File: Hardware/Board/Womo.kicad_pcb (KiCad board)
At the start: 4 copper layers, 255 x 150 mm, 465 parts, among them IC1 SPSGRFC-868, IC200 BTS6143D, IC201 BTS6143D, IC203 BTS6143D, IC204 BTS6143D, J1 USB_B_Micro, J2 Conn_ARM_JTAG_SWD_20, J3 SD_Card, J300 734-264, J301 733-368, J302 733-368, J303 733-368, J304 Truma, J305 Dormetic, J306 733-366, J307 733-366, J308 733-366, J309 733-366, J310 733-370, J311 734-163, J312 734-163, J313 734-163, J314 734-163, J315 734-168, J316 733-363, J317 RJ45_Shielded, J318 Spare, J319 SENSOR, J320 Raspberry_Pi_2_3, J321 Wasser, J322 Abwasser, J323 733-370, J324 Waveshare IoT Hat, J325 734-168, J326 733-366, J400 USB_B_Micro, J401 RJ45_Shielded, J500 SENSOR, K300 5-1393243-2, K301 5-1393243-2, K302 5-1393243-2, K303 5-1393243-2, Q100 2N7002, Q102 2N7002, Q103 2N7002, Q104 2N7002, Q200 2N7002, Q201 2N7002, Q202 2N7002, Q203 2N7002, SW1 Boot, SW3 Reset, U1 STM32L476ZGTx, U100 MAX17572, U101 MAX17572, U102 MAX17572, U104 MAX17574, U105 MAX17574, U2 M25Q128A, U200 SN74LV4052A, U201 TJA1029T, U202 TJA1029T, U203 TJA1029T, U204 TJA1029T, U205 SN74LV4052A, U206 SN74LV4052A, U207 MAX3072E, U208 MAX3072E, U209 MAX3072E, U210 MAX3072E, U211 MAX11615, U212 PCF8574A, U213 TJA1049T-3, U214 DS2482S-800+, U215 SN74LV4052A, U216 Si8642BB-B-IS1, U217 Si8642BB-B-IS1, U3 24AA02UID, U300 max4896atp+, U301 max4896atp+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

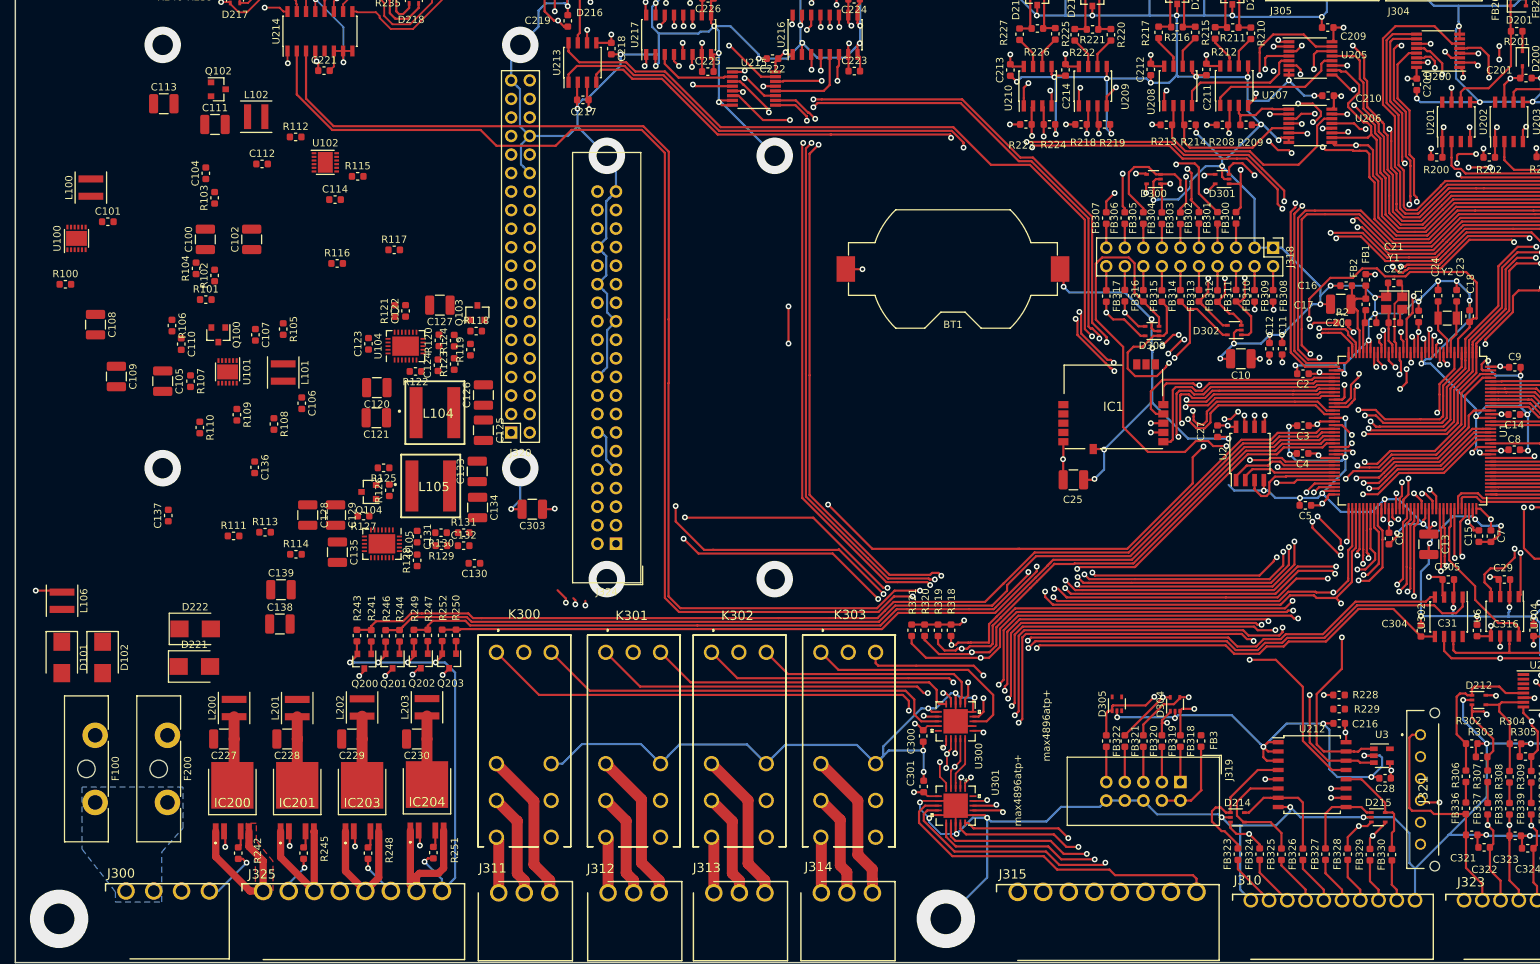
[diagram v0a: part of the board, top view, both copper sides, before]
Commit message: Power Supply gerouted, Fehlerkorrektur
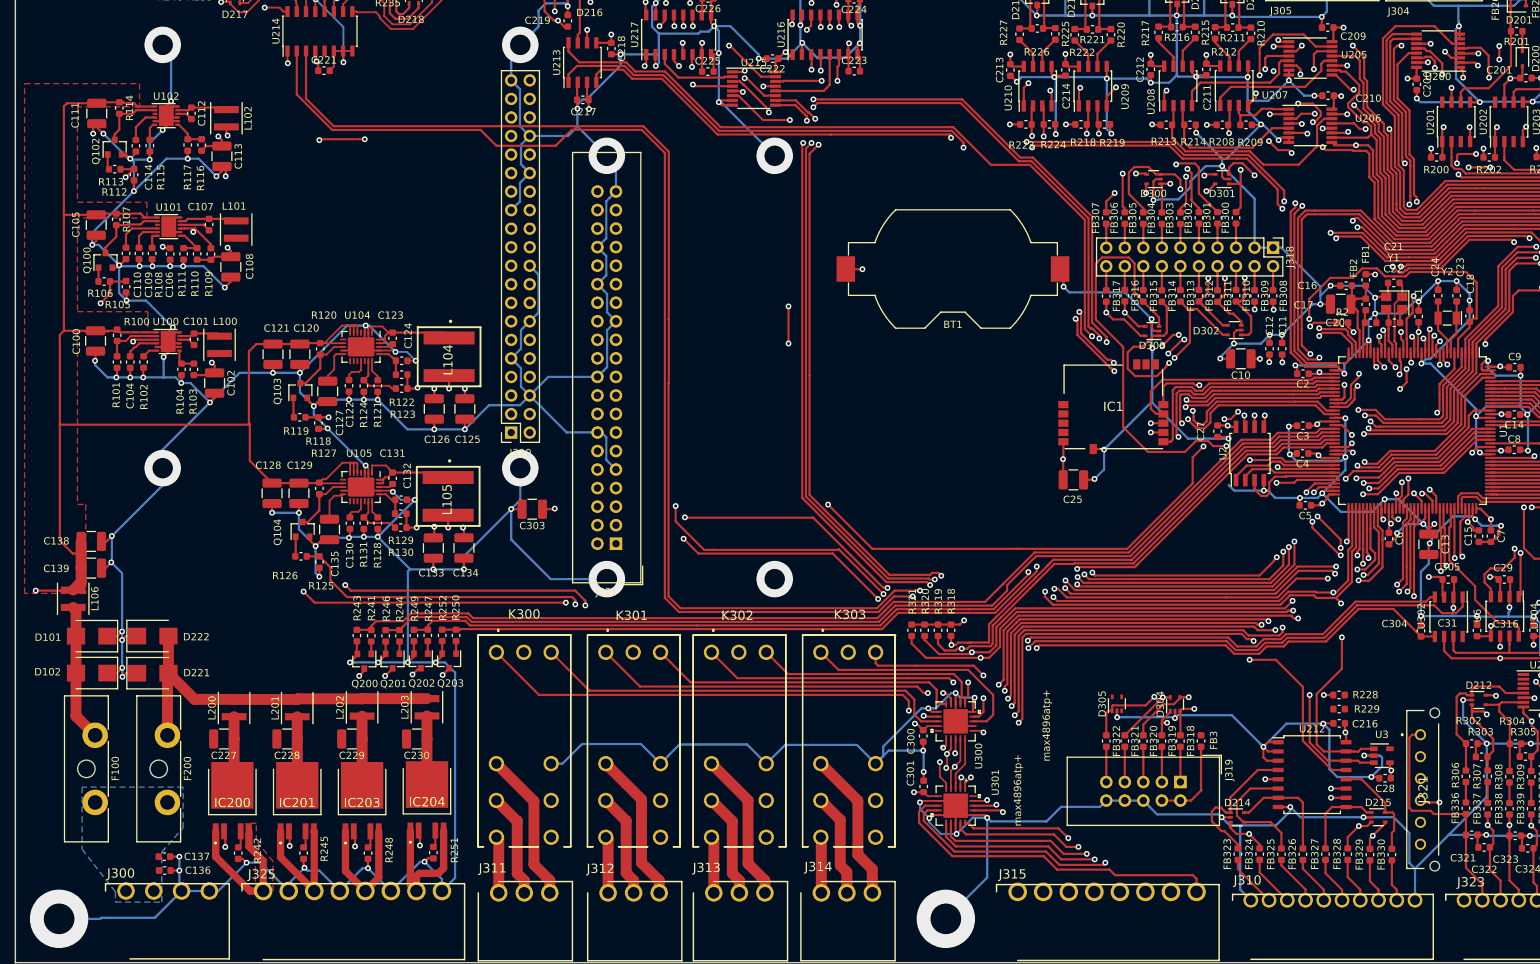
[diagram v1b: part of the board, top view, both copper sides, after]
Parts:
- C109: footprint Capacitor_SMD:C_1210_3225Metric -> Capacitor_SMD:C_0603_1608Metric
- moved R114 65.8 mm to (149.3, 157.9), turned to 270 degrees
- moved C136 56.6 mm to (155.5, 262.4), turned to 0 degrees
- moved R113 53.8 mm to (148.6, 166.3)
- moved C137 46.7 mm to (155.4, 260.5), turned to 0 degrees
- moved R111 39.3 mm to (158.1, 177.9), turned to 270 degrees
- moved R117 31.7 mm to (158.6, 163.0), turned to 270 degrees
- moved R115 28.8 mm to (153.4, 163.0), turned to 270 degrees
- moved R108 28.7 mm to (153.7, 177.8)
- moved C114 28.3 mm to (151.5, 163.1), turned to 270 degrees
- moved C138 28.2 mm to (145.4, 217.3)
- moved C104 27.9 mm to (150.7, 192.7), turned to 270 degrees
- moved L100 27.8 mm to (163.0, 190.4), turned to 270 degrees
- moved C106 27.3 mm to (156.2, 177.9)
- moved Q103 26.5 mm to (174.1, 196.6)
- moved C139 26.2 mm to (145.4, 220.9)
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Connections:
- C124 pad 1: +5VD -> Net-(C124-Pad1)
- C132 pad 1: +5VL -> Net-(C132-Pad1)
- R122 pad 2: Net-(R122-Pad2) -> Net-(C124-Pad1)
- R129 pad 2: Net-(R129-Pad2) -> Net-(C132-Pad1)
- U104 pad 20: Net-(R122-Pad2) -> Net-(C124-Pad1)
- U105 pad 20: Net-(R129-Pad2) -> Net-(C132-Pad1)
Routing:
- net GND: track 1870.1 -> 2426.8 mm, vias 172 -> 230
- net +BATT: track 655.6 -> 853.3 mm
- net 3VA_EN: track 157.7 -> 269.9 mm, vias 3 -> 4
- net 5V_EN: track 119.1 -> 218.6 mm, vias 2 -> 4
- net 5V_Raspi_EN: track 126.1 -> 187.0 mm, vias 4 -> 6
- net +3V3: track 521.6 -> 580.0 mm, vias 25 -> 28
- net PWR_Reset: track 122.0 -> 177.7 mm, vias 1 -> 2
- net Net-(D221-Pad2): track 0.00 -> 50.6 mm
- net +5V: track 195.5 -> 243.0 mm, vias 4 -> 5
- net 5V_GSM_EN: track 129.0 -> 168.9 mm
- net +5VL: track 0.00 -> 35.6 mm, vias 0 -> 4
- net +5VD: track 0.00 -> 27.3 mm, vias 0 -> 4
- net +3.3VA: track 822.6 -> 846.2 mm, vias 47 -> 49
- net Net-(D101-Pad2): track 0.00 -> 18.8 mm
- net Net-(C131-Pad1): track 0.00 -> 15.7 mm
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- added copper zone on F.Cu, net GND

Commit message: Masse und Power Flächen gerouted, bis auf Tochterboards alles komplett gerouted
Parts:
- J317, J401: footprint Connector_RJ:RJ45_Amphenol_RJHSE5380 -> Connector_RJ:RJ45_Hanrun_HR911105A
- moved J322 12.7 mm to (373.3, 240.3), turned to 0 degrees
- moved J317 9.74 mm to (363.9, 257.3)
- moved J401 9.15 mm to (405.3, 209.4)
- moved FB332 8.18 mm to (367.1, 246.8), turned to 180 degrees
- moved D306 7.82 mm to (363.4, 247.8), turned to 180 degrees
- moved R300 5.57 mm to (367.5, 251.7)
- moved C306 5.52 mm to (370.2, 250.9)
- moved R301 5.50 mm to (372.8, 251.7)
- moved FB331 4.19 mm to (367.0, 248.8), turned to 180 degrees
- moved C402 3.46 mm to (412.1, 263.0), turned to 270 degrees
- moved C401 0.71 mm to (403.9, 262.9)
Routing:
- net GND: track 2426.8 -> 2678.8 mm, vias 230 -> 243
- net +3V3: track 580.0 -> 438.7 mm, vias 28 -> 27
- net +3.3VA: track 846.2 -> 751.9 mm, vias 49 -> 51
- net +BATT: track 853.3 -> 789.1 mm, vias 6 -> 7
- net CTRL_BUS_H: track 0.00 -> 33.2 mm
- net DC_Input: track 0.00 -> 26.7 mm
- net CTRL_BUS_L: track 11.6 -> 37.1 mm
- net +5VD: track 27.3 -> 50.5 mm
- net Net-(C400-Pad1): track 0.00 -> 21.7 mm, vias 0 -> 1
- net Net-(C325-Pad1): track 40.8 -> 59.2 mm
- net CTRL_H: track 39.0 -> 57.4 mm, vias 0 -> 2
- net Net-(C326-Pad1): track 34.4 -> 51.9 mm
- net CTRL_L: track 42.0 -> 59.3 mm
- net Net-(C327-Pad1): track 29.8 -> 46.7 mm
- net Net-(C328-Pad1): track 23.5 -> 38.4 mm, vias 0 -> 1
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- added copper zone on F.Cu, net +3.3VA
- added copper zone on In2.Cu, net +3.3VA
- added copper zone on F.Cu, net +3V3
- added copper zone on In2.Cu, net +3V3
- added copper zone on F.Cu, net +5V
- added copper zone on In2.Cu, net +5V
- added copper zone on F.Cu, net +5VD
- added copper zone on In2.Cu, net +5VD
- added copper zone on F.Cu, net +5VL
- added copper zone on In2.Cu, net +5VL
- added copper zone on F.Cu, net +BATT
- added copper zone on In2.Cu, net +BATT
- added copper zone on F.Cu, net DC_Input
- added copper zone on B.Cu, net GND
- added copper zone on F.Cu, net Net-(C123-Pad1)
- added copper zone on F.Cu, net Net-(C131-Pad1)
- added copper zone on F.Cu, net Net-(D101-Pad2)
- added copper zone on F.Cu, net Net-(D221-Pad2)
- added copper zone on F.Cu, net VBB_1
- added copper zone on F.Cu, net VBB_2
- added copper zone on F.Cu, net VBB_3
- added copper zone on F.Cu, net VBB_4
- removed copper zone on B.Cu, net DC_Input

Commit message: Layout abgeschlossen, DRC durch geführt, V1.0 fertig zum review
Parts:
- added REF**: OSHW-Logo2_9.8x8mm_SilkScreen, Symbol:OSHW-Logo2_9.8x8mm_SilkScreen, F.Cu at (261.7, 204.1)
- added REF**: Symbol_GNU-Logo_SilkscreenTop, Symbol:Symbol_GNU-Logo_SilkscreenTop, F.Cu at (233.4, 202.2)
- added REF**: KiCad-Logo2_5mm_SilkScreen, Symbol:KiCad-Logo2_5mm_SilkScreen, F.Cu at (170.4, 231.6)
- C504: footprint Capacitor_SMD:C_0603_1608Metric -> Capacitor_SMD:C_1210_3225Metric
- moved C504 52.7 mm to (402.5, 142.8)
- moved C502 49.2 mm to (409.1, 149.4), turned to 0 degrees
- moved C503 48.3 mm to (405.6, 142.2)
- moved C505 47.9 mm to (402.9, 147.5), turned to 270 degrees
- moved C501 46.3 mm to (401.8, 154.6), turned to 270 degrees
- moved U501 44.5 mm to (406.4, 146.9), turned to 270 degrees
- moved C500 41.3 mm to (411.2, 154.6), turned to 270 degrees
- moved U500 38.6 mm to (406.5, 153.9)
- moved R503 38.0 mm to (405.2, 159.5), turned to 0 degrees
- moved R502 32.5 mm to (405.2, 157.5), turned to 0 degrees
- moved J500 17.2 mm to (401.5, 167.4)
- moved C404 9.07 mm to (410.6, 239.0)
- moved FB402 9.01 mm to (407.0, 222.7)
- moved C401 8.21 mm to (398.8, 256.4)
- moved FB401 7.65 mm to (405.0, 222.7)
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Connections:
- J401 pad SH: Net-(J401-PadSH) -> GND
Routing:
- net GND: track 2678.8 -> 3005.2 mm, vias 243 -> 264
- net +3.3VA: track 751.9 -> 847.9 mm, vias 51 -> 56
- net I2C3_SCL: track 213.8 -> 305.5 mm, vias 7 -> 8
- net I2C3_SDA: track 217.7 -> 303.7 mm, vias 7 -> 10
- net CTRL_BUS_L: track 37.1 -> 106.9 mm
- net INT_1_XL: track 166.2 -> 229.1 mm, vias 4 -> 6
- net IO_INT: track 169.0 -> 108.0 mm, vias 6 -> 4
- net INt_2_XL: track 162.5 -> 220.0 mm, vias 4 -> 6
- net CTRL_BUS_H: track 33.2 -> 90.4 mm
- net INT_MAG_DRDY: track 163.8 -> 213.5 mm, vias 4 -> 6
- net Net-(C402-Pad1): track 7.12 -> 49.7 mm
- net Net-(C303-Pad1): track 151.3 -> 175.4 mm
- net Net-(D400-Pad2): track 0.00 -> 18.8 mm
- net Net-(D400-Pad1): track 0.00 -> 18.6 mm
- net Net-(C400-Pad1): track 21.7 -> 36.8 mm, vias 1 -> 2
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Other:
- board size 255 x 150 mm -> 285 x 150 mm
- board text added: "(c) RFguy 11/2019"
- board text added: "1Wire 1-4"
- board text added: "1Wire 5-8"
- board text added: "Analog in"
- board text added: "Boot"
- board text added: "CAN"
- board text added: "Control"
- board text added: "DC IN"
- board text added: "Debug"
- board text added: "Digital I/O"
- board text added: "Dormetic"
- board text added: "EXT Relay 1-8"
- board text added: "Ext."
- board text added: "High Side SW 1-4"
- board text added: "K1"
- board text added: "K2"
- board text added: "K3"
- board text added: "K4"
- board text added: "LIN 1-4"
- board text added: "Modem + GNSS"
- board text added: "RS485 1-2"
- board text added: "RS485 3-4"
- board text added: "Raspberry"
- board text added: "Reset"
- board text added: "S-Addon"
- board text added: "Sensor"
- board text added: "TTY 1-2"
- board text added: "TTY 3-4"
- board text added: "Tank 1"
- board text added: "Tank 2"
- board text added: "Truma"
- board text added: "USB"
- board text added: "WomoLIN Degug Interface"
- board text added: "WomoLIN Project Control Board 1.0"
- board text added: "WomoLIN REV 1.0"
- board text added: "WomoLIN Sensor Board"
